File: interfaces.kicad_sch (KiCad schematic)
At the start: 23 parts

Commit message: Rename files and change title block
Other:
- company: Antmicro Ltd -> Capable Robot Components, Inc.
- title: Jetson Nano Baseboard -> Capable Jetson Carrier
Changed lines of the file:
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@@
   (paper "A3")
   (title_block
-    (title "Jetson Nano Baseboard")
-    (date "2022-02-04")
-    (rev "1.5.1")
-    (company "Antmicro Ltd")
-    (comment 1 "www.antmicro.com")
-    (comment 2 "Antmicro Ltd")
+    (title "Capable Jetson Carrier")
+    (date "2022-04-06")
+    (rev "v1.0")
+    (company "Capable Robot Components, Inc.")
+    (comment 1 "www.capablerobot.com")
+    (comment 2 "")
   )
   (junction (at 161.925 165.1) (diameter 0) (color 0 0 0 0)

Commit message: Rebuild
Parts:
- C14: value (none) -> C_100p_0402; footprint (none) -> jetson-nano-baseboard-footprints:0402-cap
- C37, C38, C46, C49, C51, C52, C68, C69, C70: value (none) -> C_100n_0402; footprint (none) -> jetson-nano-baseboard-footprints:0402-cap
- C47: value (none) -> C_10u_0603; footprint (none) -> jetson-nano-baseboard-footprints:0603-cap
- J3: value (none) -> SI-51005-F; footprint (none) -> jetson-nano-baseboard-footprints:SI-51005-F
- J8: value (none) -> ~; footprint (none) -> jetson-nano-baseboard-footprints:MDT580M01001
- NVME1: value (none) -> ~; footprint (none) -> jetson-nano-baseboard-footprints:LED0603
- R114, R115, R116: value (none) -> R_10k_0402; footprint (none) -> jetson-nano-baseboard-footprints:0402-res
- R128, R38, R40: value (none) -> R_220R_0402; footprint (none) -> jetson-nano-baseboard-footprints:0402-res
- SP7: value (none) -> 9774040151; footprint (none) -> jetson-nano-baseboard-footprints:9774060151
- TP20, TP7: value (none) -> ~; footprint (none) -> jetson-nano-baseboard-footprints:TP-R-1.5

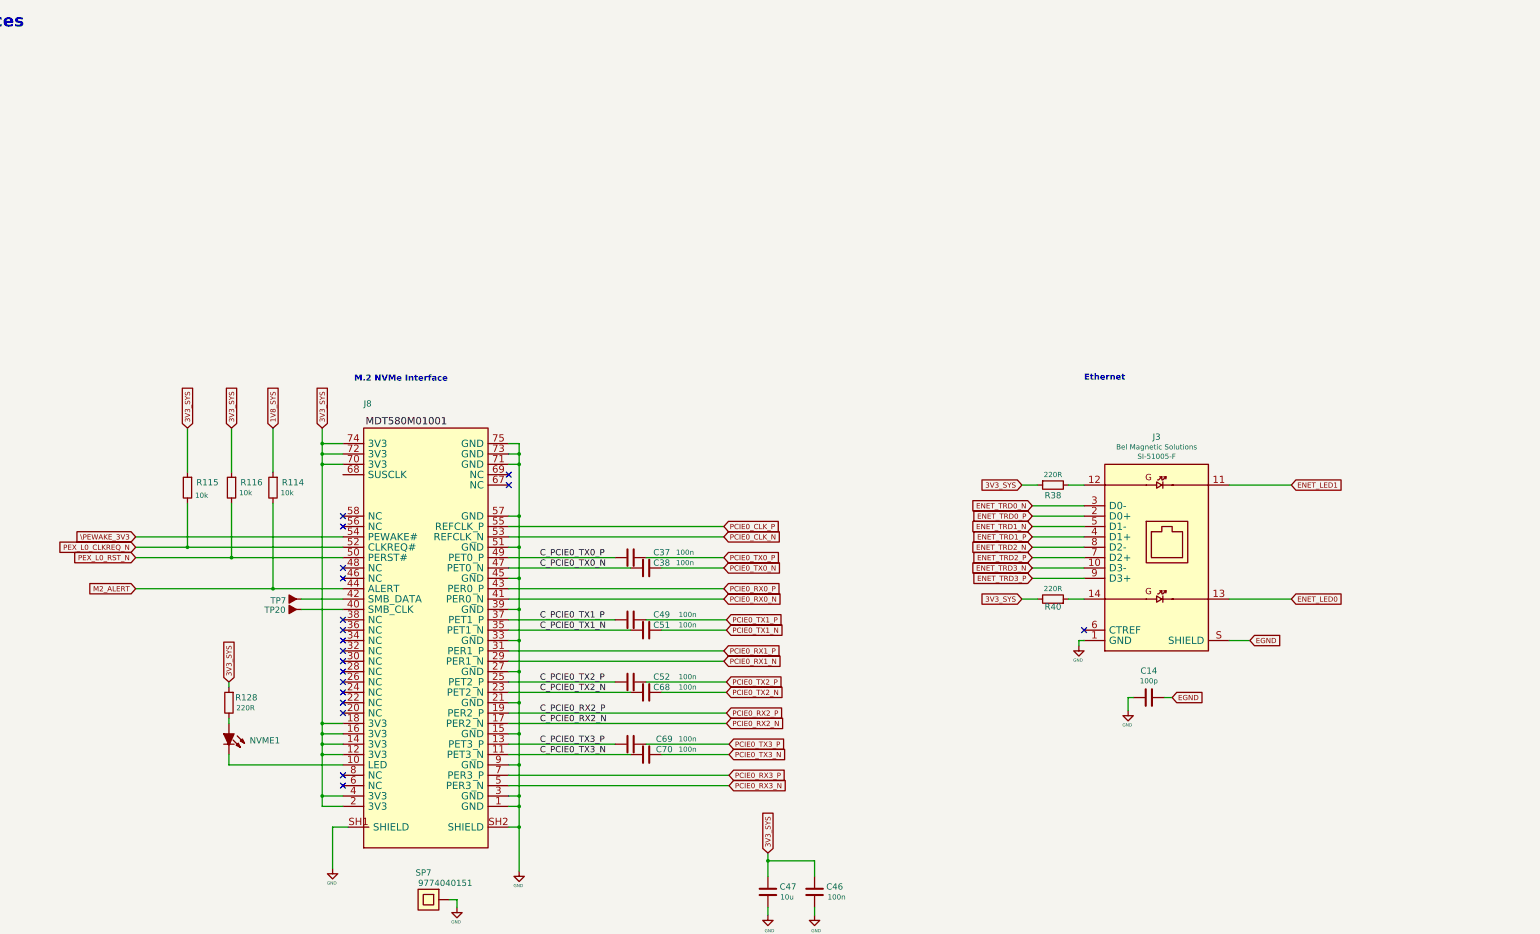
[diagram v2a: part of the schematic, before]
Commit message: Checkpoint in update of camera interfaces and overall layout
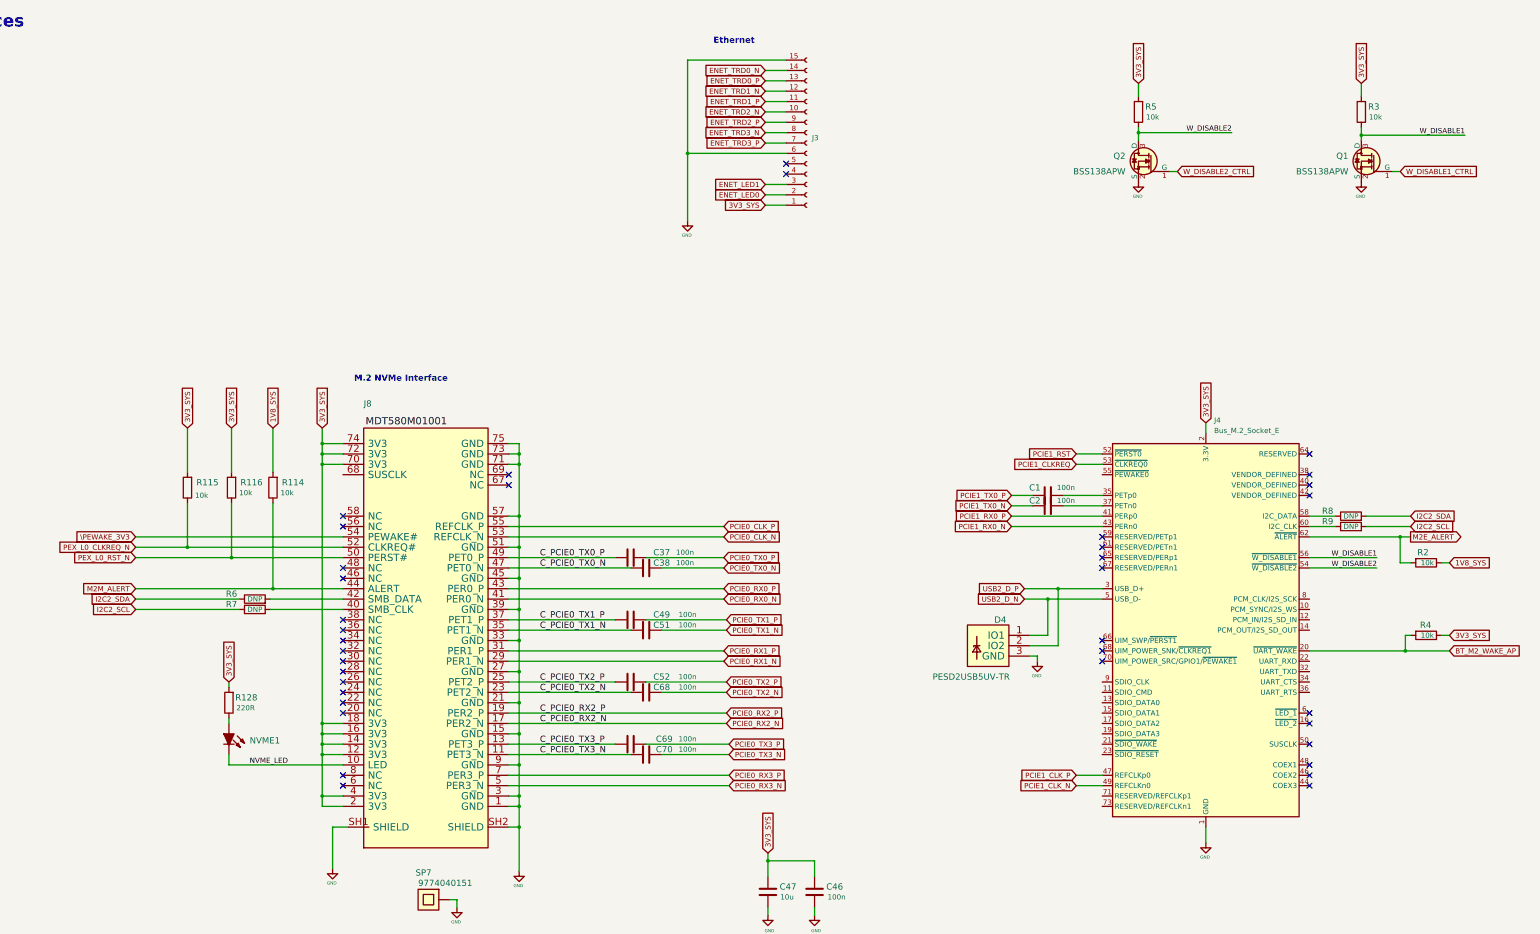
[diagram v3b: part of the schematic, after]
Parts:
- removed C14: C_100p_0402, jetson-nano-baseboard-footprints:0402-cap, symbol jetson-nano-baseboard:C_100p_0402
- removed J3: SI-51005-F, jetson-nano-baseboard-footprints:SI-51005-F, symbol jetson-nano-baseboard:SI-51005-F
- removed R38, R40: R_220R_0402, jetson-nano-baseboard-footprints:0402-res, symbol jetson-nano-baseboard:R_220R_0402
- removed TP20, TP7: ~, jetson-nano-baseboard-footprints:TP-R-1.5, symbol jetson-nano-baseboard:Testpad
- added C1, C2: C_100n_0402, jetson-nano-baseboard-footprints:0402-cap, symbol jetson-nano-baseboard:C_100n_0402
- added D4: PESD2USB5UV-TR, jetson-nano-baseboard-footprints:SOT-23s, symbol jetson-nano-baseboard:PESD2USB5UV-TR
- added J3: Conn_01x15_Female, Connector_FFC-FPC:Molex_502244-1530_1x15-1MP_P0.5mm_Horizontal, symbol Connector:Conn_01x15_Female
- added J4: Bus_M.2_Socket_E, jetson-nano-baseboard-footprints:TE_2199119-4, symbol Connector:Bus_M.2_Socket_E
- added Q1, Q2: BSS138APW, jetson-nano-baseboard-footprints:SC70-3, symbol jetson-nano-baseboard:BSS138APW
- added R2, R3, R4, R5: R_10k_0402, jetson-nano-baseboard-footprints:0402-res, symbol jetson-nano-baseboard:R_10k_0402
- added R6, R7, R8, R9: R_220R_0402, jetson-nano-baseboard-footprints:0402-res, symbol jetson-nano-baseboard:R_220R_0402
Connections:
- net 1V8_SYS: now also R2.1
- net 3V3_SYS: now also J3.1 (Pin_1), J4.2 (3.3V), J4.4 (3.3V), J4.72 (3.3V), J4.74 (3.3V), R3.2, R4.1, R5.2
- net ENET_LED0: now also J3.2 (Pin_2)
- net ENET_LED1: now also J3.3 (Pin_3)
- net ENET_TRD0_N: now also J3.14 (Pin_14)
- net ENET_TRD0_P: now also J3.13 (Pin_13)
- net ENET_TRD1_N: now also J3.12 (Pin_12)
- net ENET_TRD1_P: now also J3.11 (Pin_11)
- net ENET_TRD2_N: now also J3.10 (Pin_10)
- net ENET_TRD2_P: now also J3.9 (Pin_9)
- net ENET_TRD3_N: now also J3.8 (Pin_8)
- net ENET_TRD3_P: now also J3.7 (Pin_7)
- net GND: now also D4.3 (GND), J3.15 (Pin_15), J3.6 (Pin_6), J4.1 (GND), J4.18 (GND), J4.33 (GND), J4.39 (GND), J4.45 (GND), J4.51 (GND), J4.57 (GND), J4.63 (GND), J4.69 (GND), J4.7 (GND), J4.75 (GND), Q1.2 (S), Q2.2 (S)
- net at J8.40 (SMB_CLK): now also R7.2
- net at J8.42 (SMB_DATA): now also R6.2
- net NVME_LED: now reaches J8.10 (LED), NVME1.K
- net M2_ALERT renamed M2M_ALERT
- new net: J4.60 (I2C_CLK), R9.1
- new net: C2.2, J4.37 (PETn0)
- new net: C1.2, J4.35 (PETp0)
- new net: J4.58 (I2C_DATA), R8.1
- new net BT_M2_WAKE_AP: J4.20 (~{UART_WAKE}), R4.2
- new net I2C2_SCL: R7.1, R9.2
- new net I2C2_SDA: R6.1, R8.2
- new net M2E_ALERT: J4.62 (~{ALERT}), R2.2
- new net PCIE1_CLKREQ: J4.53 (~{CLKREQ0})
- new net PCIE1_CLK_N: J4.49 (REFCLKn0)
- new net PCIE1_CLK_P: J4.47 (REFCLKp0)
- new net PCIE1_RST: J4.52 (~{PERST0})
- new net PCIE1_RX0_N: J4.43 (PERn0)
- new net PCIE1_RX0_P: J4.41 (PERp0)
- new net PCIE1_TX0_N: C2.1
- new net PCIE1_TX0_P: C1.1
- new net USB2_D_N: D4.1 (IO1), J4.5 (USB_D-)
- new net USB2_D_P: D4.2 (IO2), J4.3 (USB_D+)
- new net W_DISABLE1: J4.56 (~{W_DISABLE1}), Q1.3 (D), R3.1
- new net W_DISABLE1_CTRL: Q1.1 (G)
- new net W_DISABLE2: J4.54 (~{W_DISABLE2}), Q2.3 (D), R5.1
- new net W_DISABLE2_CTRL: Q2.1 (G)
- no-connect marks 19 -> 37

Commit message: Update symbol library to v6
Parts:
- R6, R7, R8, R9: Val DNP -> 220R
- SP7: footprint jetson-nano-baseboard-footprints:9774060151 -> jetson-nano-baseboard-footprints:M2.5-4mm
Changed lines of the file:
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@@
       (effects (font (size 1.524 1.524)) (justify right top))
     )
-    (property "Footprint" "jetson-nano-baseboard-footprints:9774060151" (id 2) (at 137.16 241.3 0)
+    (property "Footprint" "jetson-nano-baseboard-footprints:M2.5-4mm" (id 2) (at 137.16 241.3 0)
       (effects (font (size 1.524 1.524)) hide)
     )
@@
       (effects (font (size 1.524 1.524)) (justify left) hide)
     )
-    (property "Val" "DNP" (id 6) (at 365.76 144.78 0))
+    (property "Val" "220R" (id 6) (at 365.76 144.78 0))
     (pin "1")
     (pin "2")
@@
       (effects (font (size 1.524 1.524)) (justify left) hide)
     )
-    (property "Val" "DNP" (id 6) (at 97.155 162.56 0))
+    (property "Val" "220R" (id 6) (at 97.155 162.56 0))
     (pin "1")
     (pin "2")
@@
       (effects (font (size 1.524 1.524)) (justify left) hide)
     )
-    (property "Val" "DNP" (id 6) (at 97.155 165.1 0))
+    (property "Val" "220R" (id 6) (at 97.155 165.1 0))
     (pin "1")
     (pin "2")
@@
       (effects (font (size 1.524 1.524)) (justify left) hide)
     )
-    (property "Val" "DNP" (id 6) (at 365.76 142.24 0))
-    (pin "1")
-    (pin "2")
+    (property "Val" "220R" (id 6) (at 365.76 142.24 0))
+    (pin "1")
+    (pin "2")

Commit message: Checkpoint.  New camera connectors.  Change to 2242 NVMe drive (not routed yet).
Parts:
- added N1: E Key 2230, jetson-nano-baseboard-footprints:M2outline-2230, symbol jetson-nano-baseboard:m2_outline
- added N4: (no value), symbol jetson-nano-baseboard:m2_outline
- added SP1: 9774015151R, jetson-nano-baseboard-footprints:M2.5-2.5mm, symbol jetson-nano-baseboard:9774040151
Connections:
- net GND: now also SP1.1
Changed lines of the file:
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@@
+    (stroke (width 0) (type default) (color 0 0 0 0))
+  )
+  (wire (pts (xy 365.76 238.125) (xy 365.76 240.03))
     (stroke (width 0) (type default) (color 0 0 0 0))
   )
@@
   )
   (wire (pts (xy 159.385 165.1) (xy 161.925 165.1))
+    (stroke (width 0) (type default) (color 0 0 0 0))
+  )
+  (wire (pts (xy 363.855 238.125) (xy 365.76 238.125))
     (stroke (width 0) (type default) (color 0 0 0 0))
   )
@@
     (pin "1")
   )
+  (symbol (lib_id "jetson-nano-baseboard:9774040151") (at 358.775 238.125 180) (unit 1)
+    (in_bom yes) (on_board yes)
+    (property "Reference" "SP1" (id 0) (at 355.6 232.41 0)
+      (effects (font (size 1.524 1.524)) (justify right top))
+    )
+    (property "Value" "9774015151R" (id 1) (at 356.235 234.95 0)
+      (effects (font (size 1.524 1.524)) (justify right top))
+    )
+    (property "Footprint" "jetson-nano-baseboard-footprints:M2.5-2.5mm" (id 2) (at 356.235 243.205 0)
+      (effects (font (size 1.524 1.524)) hide)
+    )
+    (property "Datasheet" "" (id 3) (at 356.235 243.205 0)
+      (effects (font (size 1.524 1.524)) hide)
+    )
+    (property "Manufacturer" "Wurth Elektronik" (id 4) (at 358.775 238.125 0)
+      (effects (font (size 1.27 1.27)) hide)
+    )
+    (property "MPN" "9774015151R" (id 5) (at 358.775 238.125 0)
+      (effects (font (size 1.27 1.27)) hide)
+    )
+    (pin "1")
+  )
   (symbol (lib_id "jetson-nano-baseboard:R_220R_0402") (at 365.76 144.78 0) (unit 1)
     (in_bom yes) (on_board yes)
@@
     (pin "2")
     (pin "3")
+  )
+  (symbol (lib_id "jetson-nano-baseboard:m2_outline") (at 327.025 237.49 0) (unit 1)
+    (in_bom no) (on_board yes)
+    (property "Reference" "N1" (id 0) (at 337.947 237.49 0))
+    (property "Value" "E Key 2230" (id 1) (at 342.392 240.03 0))
+    (property "Footprint" "jetson-nano-baseboard-footprints:M2outline-2230" (id 2) (at 327.533 243.586 0)
+      (effects (font (size 1.27 1.27)) hide)
+    )
+    (property "Datasheet" "" (id 3) (at 327.025 237.49 0)
+      (effects (font (size 1.27 1.27)) hide)
+    )
   )
   (symbol (lib_id "jetson-nano-baseboard:GND") (at 330.2 222.25 0) (unit 1)
@@
     (pin "1")
   )
+  (symbol (lib_id "jetson-nano-baseboard:GND") (at 365.76 240.03 0) (unit 1)
+    (in_bom yes) (on_board yes)
+    (property "Reference" "#GND_010" (id 0) (at 365.76 240.03 0)
+      (effects (font (size 0.508 0.508)) hide)
+    )
+    (property "Value" "GND" (id 1) (at 365.5568 243.586 0)
+      (effects (font (size 0.762 0.762)))
+    )
+    (property "Footprint" "" (id 2) (at 365.76 240.03 0)
+      (effects (font (size 1.778 1.778)) hide)
+    )
+    (property "Datasheet" "" (id 3) (at 365.76 240.03 0)
+      (effects (font (size 1.778 1.778)) hide)
+    )
+    (pin "1")
+  )
   (symbol (lib_id "jetson-nano-baseboard:R_10k_0402") (at 384.175 171.45 180) (unit 1)
     (in_bom yes) (on_board yes)
@@
     (pin "2")
   )
+  (symbol (lib_id "jetson-nano-baseboard:m2_outline") (at 132.08 247.65 0) (unit 1)
+    (in_bom no) (on_board yes)
+    (property "Reference" "N4" (id 0) (at 143.002 247.65 0))
+    (property "Value" "" (id 1) (at 147.447 250.19 0))
+    (property "Footprint" "" (id 2) (at 132.588 253.746 0)
+      (effects (font (size 1.27 1.27)) hide)
+    )
+    (property "Datasheet" "" (id 3) (at 132.08 247.65 0)
+      (effects (font (size 1.27 1.27)) hide)
+    )
+  )
   (symbol (lib_id "jetson-nano-baseboard:C_100n_0402") (at 291.465 137.16 90) (unit 1)
